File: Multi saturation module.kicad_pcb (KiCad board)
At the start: 2 copper layers, 56 parts, among them J1 Audio_in, J2 Mix_CV_in, J3 Mix_audio_out, J4 Dry_audio_out, J5 Wet_audio_out, J6 EURO_PWR_2x5, J7 EuroPower_JST_3P, SW1 Bypass_sw_DPDT, SW2 Bypass_sw_DPDT, SW3 SW_SPST, T1 TL016-R, U1 NE5532, U2 NE5532, U3 VTL5C, U4 NE5532, U5 NE5532, U6 VTL5C

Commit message: Separate boards branch started
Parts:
- moved D1 215.1 mm to (234.6, 138.2)
- moved SW2 206.3 mm to (252.8, 127.4)
- moved J1 195.9 mm to (222.8, 106.6)
- moved J2 195.9 mm to (233.8, 106.6)
- moved J3 195.9 mm to (244.9, 106.6)
- moved J4 195.9 mm to (255.9, 106.6)
- moved J5 195.9 mm to (267.0, 106.6)
- moved C3 178.0 mm to (126.4, 37.4)
- moved U4 172.3 mm to (160.0, 17.8)
- moved U5 172.3 mm to (171.6, 17.8)
- moved U3 171.0 mm to (117.8, 30.4)
- moved R4 155.3 mm to (106.7, 19.0)
- moved R5 155.3 mm to (106.7, 23.1)
- moved R7 154.5 mm to (106.7, 27.1)
- moved U6 152.6 mm to (159.7, 29.1)
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
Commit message: Laid out footprints on three boards
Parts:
- removed J3: Mix_audio_out, DIYSynthMNL:AudioJack_3.5mm_long_pads
- added C6: 0.1uF, DIYSynthMNL:C_Rect_L7.0mm_W2.0mm_P5.00mm_BigPads, F.Cu at (143.8, 118.2)
- added C7: 0.1uF, DIYSynthMNL:C_Rect_L7.0mm_W2.0mm_P5.00mm_BigPads, F.Cu at (127.0, 94.2)
- added C8: 22uF, DIYSynthMNL:CP_Radial_D4.0mm_P1.50mm, F.Cu at (121.5, 110.2)
- added C9: 22uF, DIYSynthMNL:CP_Radial_D4.0mm_P1.50mm, F.Cu at (126.3, 110.2)
- added J10: Board_A_1, Connector_PinHeader_2.54mm:PinHeader_1x16_P2.54mm_Vertical, F.Cu at (110.0, 45.0)
- added J11: Board_A_2, Connector_PinHeader_2.54mm:PinHeader_1x16_P2.54mm_Vertical, F.Cu at (146.0, 45.0)
- added J8: Board_B_1, Connector_PinHeader_2.54mm:PinHeader_1x16_P2.54mm_Vertical, B.Cu at (152.0, 45.0)
- added J9: Board_B_2, Connector_PinHeader_2.54mm:PinHeader_1x16_P2.54mm_Vertical, B.Cu at (188.0, 45.0)
- added REF**: PanelHole_Potentiometer_RV09, DIYSynthMNL:PanelHole_Potentiometer_RV09, F.Cu at (200.0, 98.2)
- added REF**: Panel_8HP, DIYSynthMNL:Panel_8HP, F.Cu at (234.2, 15.0)
- added REF**: PanelHole_AudioJack_3.5mm, DIYSynthMNL:PanelHole_AudioJack_3.5mm, F.Cu at (198.5, 119.1)
- added REF**: PanelHole_ToggleSwitch_MTS-101, DIYSynthMNL:PanelHole_ToggleSwitch_MTS-101, F.Cu at (212.5, 41.5)
- added REF**: PanelHole_Bourns_3296W_TrimPot, DIYSynthMNL:PanelHole_Bourns_3296W_TrimPot, F.Cu at (204.5, 107.5)
- added REF**: PanelHole_AudioJack_3.5mm, DIYSynthMNL:PanelHole_AudioJack_3.5mm, F.Cu at (226.5, 119.1)
- added REF**: PanelHole_Potentiometer_RV09, DIYSynthMNL:PanelHole_Potentiometer_RV09, F.Cu at (220.0, 98.2)
- added REF**: PanelHole_AudioJack_3.5mm, DIYSynthMNL:PanelHole_AudioJack_3.5mm, F.Cu at (212.5, 119.1)
- added REF**: ToggleSwitch_MTS-202_DPDT, DIYSynthMNL:PanelHole_ToggleSwitch_MTS-202, F.Cu at (212.5, 75.5)
- added REF**: PanelHole_AudioJack_3.5mm, DIYSynthMNL:PanelHole_AudioJack_3.5mm, F.Cu at (226.5, 104.2)
- added REF**: MountingHole_M3, DIYSynthMNL:MountingHole_M3, F.Cu at (200.0, 18.0)
- added REF**: PanelHole_Bourns_3296W_TrimPot, DIYSynthMNL:PanelHole_Bourns_3296W_TrimPot, F.Cu at (196.5, 107.5)
- added REF**: ToggleSwitch_MTS-202_DPDT, DIYSynthMNL:PanelHole_ToggleSwitch_MTS-202, F.Cu at (212.5, 58.5)
- added REF**: MountingHole_M3, DIYSynthMNL:MountingHole_M3, F.Cu at (200.0, 140.5)
- C4, C5: value 22uF -> 0.1uF; footprint DIYSynthMNL:CP_Radial_D4.0mm_P1.50mm -> DIYSynthMNL:C_Rect_L7.0mm_W2.0mm_P5.00mm_BigPads
- D1: value LED -> ClipLed1
- D2: value LED -> ClipLed2
- D3, D4: value LED -> 4148; footprint DIYSynthMNL:LED_D5.0mm_BigPads -> DIYSynthMNL:D_4148_BigPads
- D5: value 4148 -> Opto_sat; footprint DIYSynthMNL:D_4148_BigPads -> DIYSynthMNL:LED_D5.0mm_BigPads
- D6: value 4148 -> Wet/Dry; footprint DIYSynthMNL:D_4148_BigPads -> DIYSynthMNL:LED_D5.0mm_BigPads
- J1: value Audio_in -> Mix_audio_out
- J2: value Mix_CV_in -> Audio_in
- J4: value Dry_audio_out -> Mix_CV_in
- J6: value EURO_PWR_2x5 -> EuroPower_JST_3P; footprint DIYSynthMNL:IDC-Header_2x05_P2.54mm_Vertical_BigPads -> DIYSynthMNL:Eurorack_power_jst_3P
- J7: value EuroPower_JST_3P -> EURO_PWR_2x5; footprint DIYSynthMNL:Eurorack_power_jst_3P -> DIYSynthMNL:IDC-Header_2x05_P2.54mm_Vertical_BigPads
- R5: value 10R -> 10k
- R6: value 100k -> 10R
- R7: value 680R -> 100k
- R8: value 10k -> 680R
- RV1: value Mix_trim_50k -> Dry_gain_10k; footprint DIYSynthMNL:Potentiometer_RV09_BigPads -> DIYSynthMNL:Potentiometer_Bourns_3296W_Vertical_BigPads
- RV3: value Dry_gain_10k -> CV_lvl_50k; footprint DIYSynthMNL:Potentiometer_Bourns_3296W_Vertical_BigPads -> DIYSynthMNL:Potentiometer_RV09_BigPads
- RV4: value CV_lvl_50k -> Mix_trim_50k
- SW1: value Bypass_sw_DPDT -> Clipping; footprint benjiaomodular:ToggleSwitch_MTS-202_DPDT -> DIYSynthMNL:ToggleSwitch_MTS-102_SPDT
- SW2: value Bypass_sw_DPDT -> Xformer_bypass; footprint benjiaomodular:ToggleSwitch_MTS-202_DPDT -> DIYSynthMNL:ToggleSwitch_MTS-202_DPDT
- SW3: value SW_SPST -> Opto_bypass; footprint benjiaomodular:ToggleSwitch_MTS-102_SPDT -> DIYSynthMNL:ToggleSwitch_MTS-202_DPDT
- moved R22 150.5 mm to (159.0, 27.7), turned to -90 degrees
- moved D3 146.8 mm to (153.0, 27.7), turned to -90 degrees
- moved D4 144.2 mm to (156.0, 35.3), turned to 90 degrees
- moved J6 142.0 mm to (122.0, 127.0)
- moved D8 130.7 mm to (128.5, 122.2), turned to 90 degrees
- moved D1 126.9 mm to (166.0, 31.5)
- moved D2 126.6 mm to (174.0, 31.5)
- moved J7 122.9 mm to (112.5, 116.5)
- moved D7 122.7 mm to (120.5, 114.9), turned to -90 degrees
- moved D5 120.5 mm to (160.0, 58.5)
- moved SW3 116.7 mm to (170.0, 58.5), turned to 180 degrees
- moved SW1 110.1 mm to (170.0, 41.5), turned to 180 degrees
- moved U4 105.8 mm to (137.6, 121.2)
- moved C4 104.6 mm to (136.3, 41.0), turned to 180 degrees
- moved C5 100.6 mm to (129.1, 70.1), turned to 180 degrees
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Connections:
- net Net-(U4A--) renamed RV2_3
- C1 pad 2: Net-(SW1B-B) -> SW1_5
- C3 pad 2: Net-(SW2B-B) -> SW2_5
- C4 pad 2: GND -> -12V
- C5 pad 1: GND -> +12V
- D2 pad 1: Net-(D2-K) -> Net-(D1-A)
- D2 pad 2: Net-(D2-A) -> Net-(D1-K)
- D3 pad 1: Net-(D2-A) -> Net-(D1-A)
- D3 pad 2: Net-(D2-K) -> GND
- D4 pad 1: Net-(D4-K) -> GND
- D4 pad 2: Net-(D4-A) -> Net-(D1-A)
- D5 pad 1: Net-(D2-A) -> D1_-
- D5 pad 2: GND -> D1_+
- D6 pad 1: GND -> D4_-
- D6 pad 2: Net-(D2-A) -> D4_+
- J1 pad T: Audio_in -> Mix_audio_out
- J2 pad T: Mix_CV_in -> Audio_in
- J4 pad T: Dry -> Mix_CV_in
- J6 pad 2: Net-(D7-A) -> GND
- J6 pad 3: GND -> Net-(D8-K)
- J7 pad 2: GND -> Net-(D7-A)
- J7 pad 3: Net-(D8-K) -> GND
- R1 pad 1: Net-(SW1A-A) -> SW1_1
- R10 pad 1: Net-(D1-K) -> D1_-
- R12 pad 1: Net-(SW2B-A) -> SW2_4
- R12 pad 2: Net-(SW2A-A) -> SW2_1
- R13 pad 1: Net-(R13-Pad1) -> RV1_2
- R15 pad 2: Net-(U4B--) -> RV3_3
- R22 pad 1: Net-(SW3-A) -> Net-(SW1-A)
- R3 pad 2: Net-(SW1B-A) -> SW1_4
- R4 pad 1: Net-(SW2A-A) -> SW2_1
- R5 pad 1: Net-(C2-Pad2) -> Net-(U1B--)
- R5 pad 2: Net-(U2B-+) -> SW2_2
- R6 pad 1: Net-(U1B-+) -> Net-(C2-Pad2)
- R6 pad 2: GND -> Net-(U2B-+)
- R7 pad 1: Net-(D1-A) -> Net-(U1B-+)
- R7 pad 2: Net-(R7-Pad2) -> GND
- R8 pad 1: Net-(U1B--) -> D1_+
- R8 pad 2: Net-(SW2A-B) -> Net-(R8-Pad2)
- RV1 pad 2: Net-(R13-Pad1) -> GND
- RV1 pad 3: +12V -> RV3_3
- RV3 pad 2: GND -> RV4_2
- RV3 pad 3: Net-(U4B--) -> Mix_CV_in
- RV4 pad 2: Net-(U5A-+) -> RV1_2
- RV4 pad 3: Mix_CV_in -> +12V
- SW1 pad 1: Net-(SW1A-A) -> Net-(SW1-A)
- SW1 pad 2: Dry -> Net-(D1-K)
- SW1 pad 3: Net-(SW1A-C) -> unconnected-(SW1-C-Pad3)
- SW2 pad 1: Net-(SW2A-A) -> SW1_1
- SW2 pad 2: Net-(SW2A-B) -> Dry
- SW2 pad 4: Net-(SW2B-A) -> SW1_4
- SW2 pad 5: Net-(SW2B-B) -> SW1_5
- SW3 pad 1: Net-(SW3-A) -> SW2_1
- SW3 pad 2: Net-(D2-K) -> SW2_2
- SW3 pad 3: unconnected-(SW3-C-Pad3) -> Net-(SW3A-C)
- T1 pad 6: Net-(SW1B-A) -> SW1_4
- U1 pad 7: Net-(SW2A-B) -> SW2_2
- U2 pad 6: Net-(D1-K) -> D1_-
- U2 pad 7: Net-(R7-Pad2) -> Net-(R8-Pad2)
- U3 pad 1: Net-(D1-K) -> D1_-
- U3 pad 2: Net-(D1-A) -> D1_+
- U3 pad 3: Net-(SW2B-A) -> SW2_4
- U4 pad 6: Net-(U4B--) -> RV3_3
- U5 pad 3: Net-(U5A-+) -> RV4_2
- U5 pad 7: Net-(D4-A) -> D4_+
- U6 pad 2: Net-(D4-K) -> D4_-
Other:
- board outline added: 124.5 x 128.5 mm

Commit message: board update
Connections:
- net Net-(D7-A) renamed /Board_A/+12V_IN
- net Net-(D8-K) renamed /Board_A/-12V_IN
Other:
- rule pad_to_mask_clearance: 0 -> 0.08

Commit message: All boards routed
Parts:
- C8, C9: footprint DIYSynthMNL:CP_Radial_D4.0mm_P1.50mm -> Capacitor_THT:CP_Radial_D5.0mm_P2.50mm
- moved C9 1.84 mm to (127.6, 111.5)
- moved D7 1.59 mm to (121.6, 116.0)
- moved D8 1.59 mm to (129.6, 123.4)
- moved J6 1.59 mm to (123.1, 128.2)
- moved C8 1.30 mm to (121.4, 111.5)
- moved J7 0.60 mm to (113.1, 116.5)
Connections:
- D3 pad 2: GND -> GND1
- D4 pad 1: GND -> GND1
- D5 pad 1: D1_- -> D1_-_B
- D5 pad 2: D1_+ -> D1_+_B
- D6 pad 1: D4_- -> D4_-_B
- D6 pad 2: D4_+ -> D4_+_B
- J1 pad S: GND -> GND1
- J1 pad T: Mix_audio_out -> Mix_audio_out_B
- J2 pad S: GND -> GND1
- J2 pad T: Audio_in -> Audio_in_B
- J4 pad S: GND -> GND1
- J4 pad T: Mix_CV_in -> Mix_CV_in_B
- J5 pad S: GND -> GND1
- J5 pad T: Wet -> Wet_B
- J8 pad 1: +12V -> +12VA
- J8 pad 10: D4_+ -> D4_+_B
- J8 pad 11: Clipping_diodes -> Clipping_diodes_B
- J8 pad 12: Mix_CV_in -> RV4_3_B
- J8 pad 13: RV4_2 -> RV4_2_B
- J8 pad 14: RV1_2 -> RV1_2_B
- J8 pad 15: RV2_3 -> RV2_3_B
- J8 pad 16: RV3_3 -> RV3_3_B
- J8 pad 2: GND -> GND1
- J8 pad 3: GND -> GND1
- J8 pad 4: GND -> GND1
- J8 pad 5: -12V -> -12VA
- J8 pad 7: D1_- -> D1_-_B
- J8 pad 8: D1_+ -> D1_+_B
- J8 pad 9: D4_- -> D4_-_B
- J9 pad 1: Dry -> SW1_2_B
- J9 pad 10: Mix_CV_in -> Mix_CV_in_B
- J9 pad 11: Mix_audio_out -> Mix_audio_out_B
- J9 pad 12: Wet -> Wet_B
- J9 pad 13: GND -> GND1
- J9 pad 14: GND -> GND1
- J9 pad 15: GND -> GND1
- J9 pad 16: GND -> GND1
- J9 pad 2: SW1_1 -> SW1_1_B
- J9 pad 3: SW1_4 -> SW1_4_B
- J9 pad 4: SW1_5 -> SW1_5_B
- J9 pad 5: SW2_2 -> SW2_2_B
- J9 pad 6: SW2_1 -> SW2_1_B
- J9 pad 7: SW2_4 -> SW2_4_B
- J9 pad 8: SW2_5 -> SW2_5_B
- J9 pad 9: Audio_in -> Audio_in_B
- R22 pad 2: Clipping_diodes -> Clipping_diodes_B
- RV1 pad 1: GND -> GND1
- RV1 pad 2: GND -> GND1
- RV1 pad 3: RV3_3 -> RV3_3_B
- RV2 pad 1: GND -> GND1
- RV2 pad 2: GND -> GND1
- RV2 pad 3: RV2_3 -> RV2_3_B
- RV3 pad 1: GND -> GND1
- RV3 pad 2: RV4_2 -> RV4_2_B
- RV3 pad 3: Mix_CV_in -> RV4_3_B
- RV4 pad 1: GND -> GND1
- RV4 pad 2: RV1_2 -> RV1_2_B
- RV4 pad 3: +12V -> +12VA
- SW2 pad 1: SW1_1 -> SW1_1_B
- SW2 pad 2: Dry -> SW1_2_B
- SW2 pad 4: SW1_4 -> SW1_4_B
- SW2 pad 5: SW1_5 -> SW1_5_B
- SW3 pad 1: SW2_1 -> SW2_1_B
- SW3 pad 2: SW2_2 -> SW2_2_B
- SW3 pad 4: SW2_4 -> SW2_4_B
- SW3 pad 5: SW2_5 -> SW2_5_B
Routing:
- net +12V: track 0.00 -> 144.8 mm, vias 0 -> 4
- net -12V: track 0.00 -> 132.0 mm, vias 0 -> 3
- net Dry: track 0.00 -> 130.0 mm, vias 0 -> 5
- net Audio_in_B: track 0.00 -> 87.4 mm, vias 0 -> 3
- net RV2_3: track 0.00 -> 83.7 mm, vias 0 -> 5
- net Clipping_diodes: track 0.00 -> 81.9 mm, vias 0 -> 4
- net RV3_3: track 0.00 -> 76.4 mm, vias 0 -> 2
- net Wet_B: track 0.00 -> 74.6 mm, vias 0 -> 4
- net Mix_audio_out_B: track 0.00 -> 72.5 mm, vias 0 -> 4
- net Wet: track 0.00 -> 72.4 mm, vias 0 -> 3
- net +12VA: track 0.00 -> 64.5 mm, vias 0 -> 2
- net Mix_CV_in: track 0.00 -> 55.4 mm, vias 0 -> 1
- net Mix_CV_in_B: track 0.00 -> 53.2 mm, vias 0 -> 3
- net D4_+_B: track 0.00 -> 53.0 mm, vias 0 -> 3
- net D4_-_B: track 0.00 -> 52.0 mm, vias 0 -> 3
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
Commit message: board routing update
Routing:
- net /Board_A/+12V_IN: track 13.0 -> 18.1 mm
- net +12V: track 144.8 -> 148.3 mm
- net +12VA: track 64.5 -> 66.0 mm

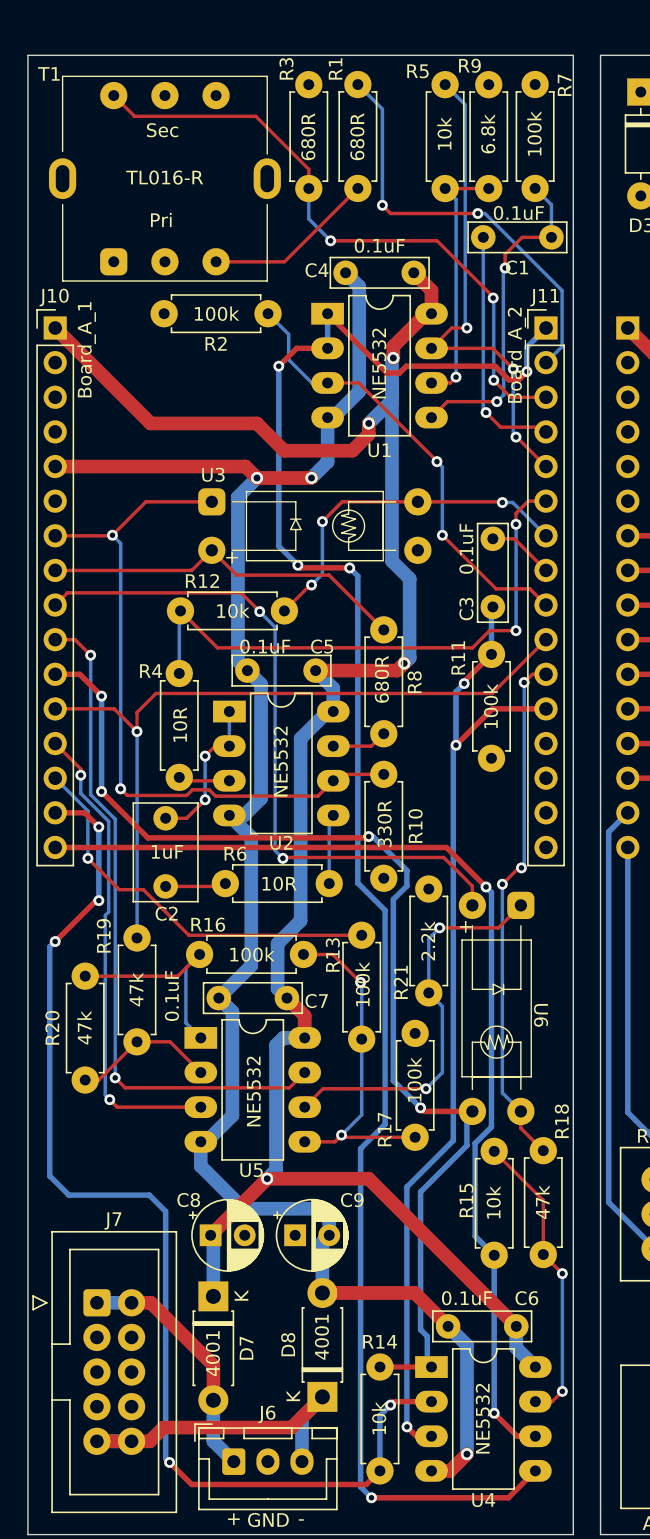
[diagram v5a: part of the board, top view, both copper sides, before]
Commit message: routing with bigger traces finished
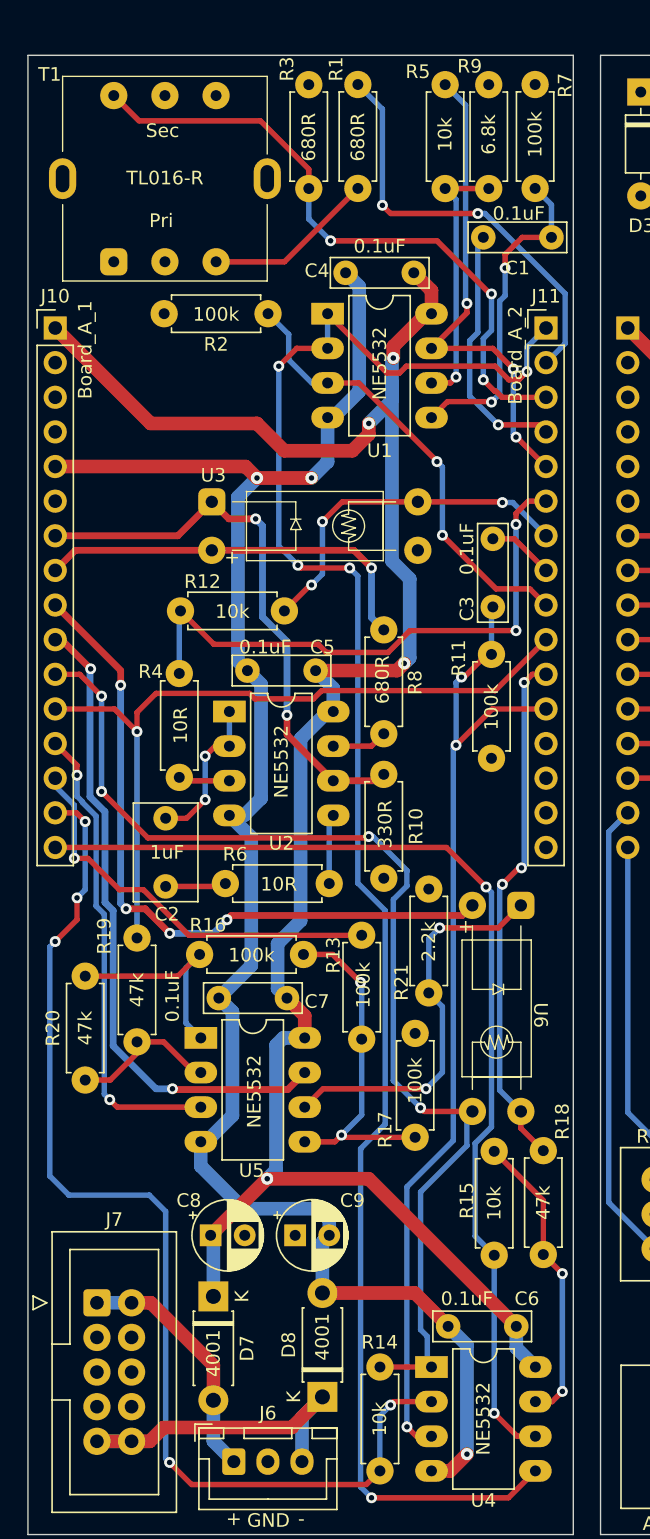
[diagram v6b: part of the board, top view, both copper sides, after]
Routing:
- net D1_-: track 51.2 -> 41.7 mm
- net D1_+: track 27.1 -> 29.3 mm, vias 0 -> 1
- net D4_+: track 49.5 -> 47.8 mm
- net RV2_3: track 83.7 -> 82.4 mm
- net SW1_4: track 46.6 -> 47.5 mm
- net SW1_5: track 17.4 -> 18.3 mm
- net SW2_2: track 36.5 -> 35.9 mm
- net RV1_2: track 29.3 -> 29.9 mm
- net D4_-: track 51.0 -> 51.4 mm, vias 2 -> 4

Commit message: board connector wrong placement fix
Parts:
- J10, J11: moved to B.Cu
- moved J8 36.0 mm to (188.0, 45.0)
- moved J9 36.0 mm to (152.0, 45.0)
- turned J10 to 180 degrees
- turned J11 to 180 degrees
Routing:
- net RV2_3_B: track 34.0 -> 60.0 mm, vias 0 -> 3
- net Mix_CV_in_B: track 53.6 -> 78.5 mm, vias 3 -> 2
- net D1_-_B: track 7.45 -> 30.0 mm
- net RV4_2_B: track 48.4 -> 26.1 mm, vias 3 -> 1
- net Clipping_diodes_B: track 39.8 -> 60.5 mm
- net RV4_3_B: track 50.6 -> 30.9 mm
- net Mix_audio_out_B: track 72.8 -> 91.1 mm, vias 4 -> 1
- net D1_+_B: track 12.3 -> 29.8 mm
- net RV3_3_B: track 33.6 -> 50.8 mm, vias 0 -> 3
- net Audio_in_B: track 87.4 -> 70.9 mm, vias 3 -> 1
- net RV1_2_B: track 27.2 -> 41.9 mm, vias 1 -> 3
- net Wet_B: track 74.6 -> 82.0 mm, vias 4 -> 1
- net D4_+_B: track 53.3 -> 46.3 mm, vias 3 -> 2
- net SW2_1_B: track 18.0 -> 24.8 mm, vias 1 -> 2
- net SW2_4_B: track 23.0 -> 16.8 mm, vias 1 -> 0
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- added copper zone on B.Cu, net GND
- added copper zone on F.Cu, net GND
- added copper zone on B.Cu, net GND1
- added copper zone on F.Cu, net GND1

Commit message: board update
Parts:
- added REF**: MountingHole_M3_Standoff, DIYSynthMNL:MountingHole_M3_Standoff, F.Cu at (116.0, 51.4)
- added REF**: MountingHole_M3_Standoff, DIYSynthMNL:MountingHole_M3_Standoff, F.Cu at (140.0, 81.3)
- added REF**: MountingHole_M3_Standoff, DIYSynthMNL:MountingHole_M3_Standoff, F.Cu at (182.0, 51.4)
- added REF**: MountingHole_M3_Standoff, DIYSynthMNL:MountingHole_M3_Standoff, F.Cu at (158.0, 81.3)
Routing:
- net SW1_4_B: track 40.3 -> 38.2 mm
- net -12V: track 132.0 -> 134.0 mm
- net Mix_CV_in_B: track 78.5 -> 80.2 mm
- net Wet: track 72.4 -> 73.1 mm, vias 3 -> 2
- net GND: vias 0 -> 5
